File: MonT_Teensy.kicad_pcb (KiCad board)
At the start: 2 copper layers, 61.2 x 18 mm, 11 parts, among them J1 Teensy, J2 DB25_Male, U1 MAX3232

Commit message: teensy renders
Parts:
- J1: footprint 0_LOCAL:Teensy35_36_MonT -> 0_LOCAL:Teensy35_36_MonT_c

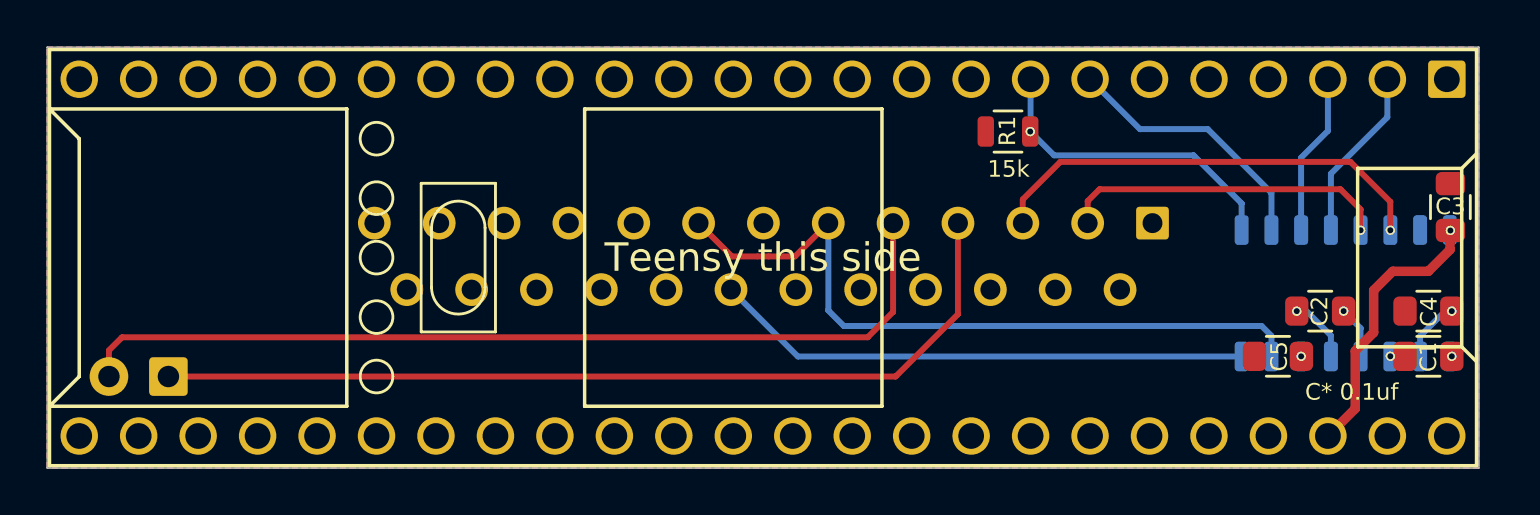
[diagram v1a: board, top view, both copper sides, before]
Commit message: boms and remove dsr pulldown
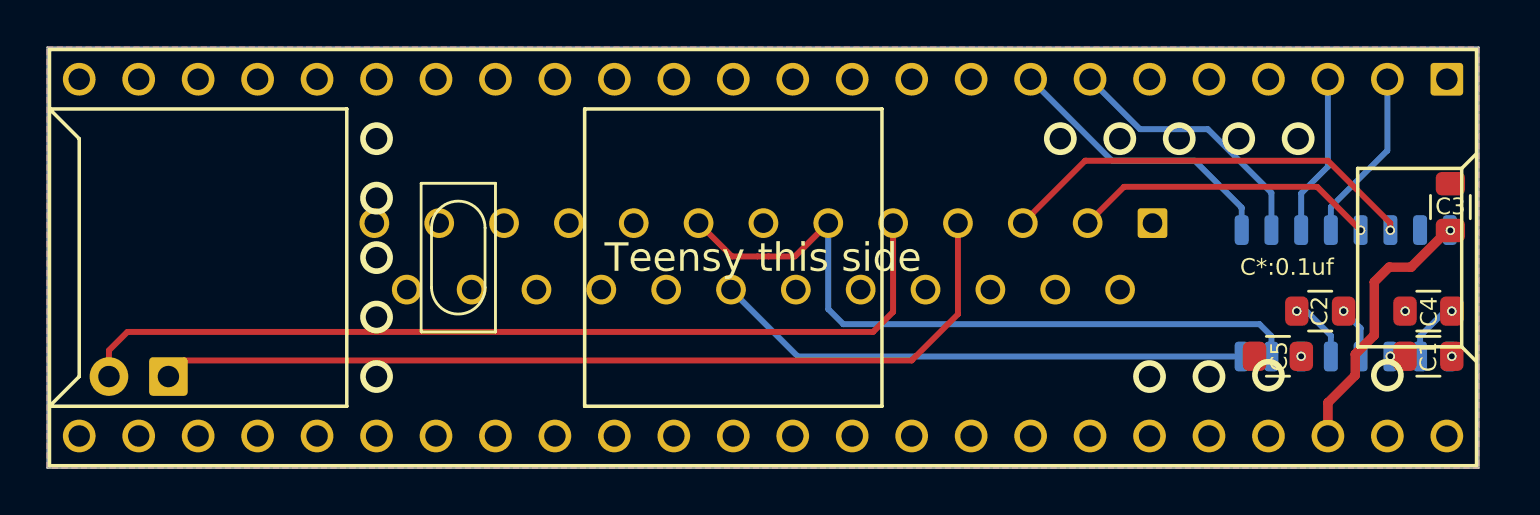
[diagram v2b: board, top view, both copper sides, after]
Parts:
- removed R1: 15k, 0_LOCAL:R_0805
- J1: footprint 0_LOCAL:Teensy35_36_MonT_c -> 0_LOCAL:Teensy35_36_MonT
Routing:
- net /DSR_TTL: track 13.7 -> 12.2 mm, vias 1 -> 0
- net /RXD: track 19.3 -> 18.2 mm
- net /TXD: track 14.1 -> 13.1 mm
- net GND: vias 0 -> 1
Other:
- board text added: "C*:0.1uf"
- board text removed: "C* 0.1uf"

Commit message: remove dsr pulldown
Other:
- board text added: "C1-C5 0.1uf"
- board text removed: "C*:0.1uf"
